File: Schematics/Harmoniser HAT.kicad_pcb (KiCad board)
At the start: 2 copper layers, 98 x 55 mm, 129 parts, among them J1 RPi GPIO, J2 Line In, J3 Inst In, J4 Line Out, J5 Inst Out, J6 I2C Header, J7 PWR, J8 I2S Header, Q1 BC547, Q1 Q_NPN_BEC, Q2 BC547, Q2 Q_NPN_BEC, SW1 RotaryEncoder_Switch, SW2 RotaryEncoder_Switch, SW3 RotaryEncoder_Switch, SW4 RotaryEncoder_Switch, U1 PCM3060, U2 24LC256, U3 Opamp_Dual, U4 Opamp_Dual, U5 PCA9555PW

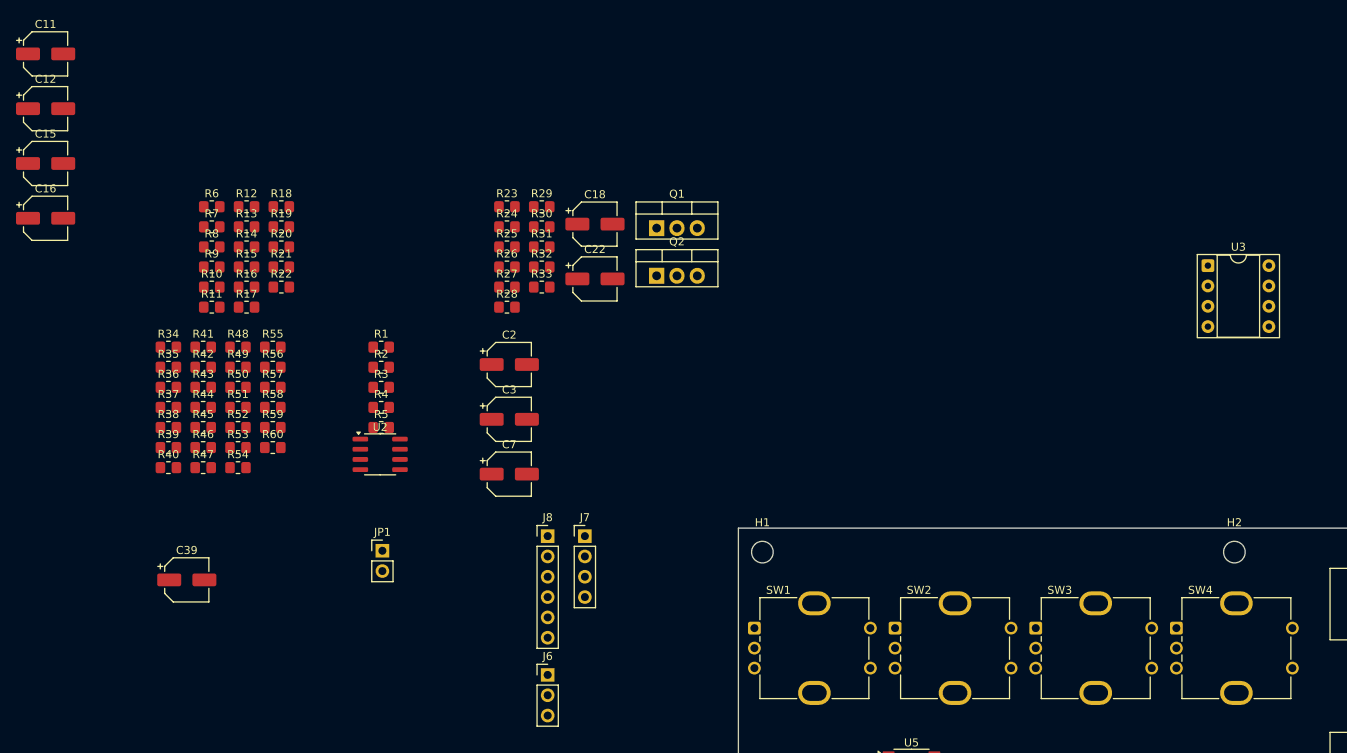
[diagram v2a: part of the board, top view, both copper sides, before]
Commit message: Changed footprints, added 3d model to GPIO
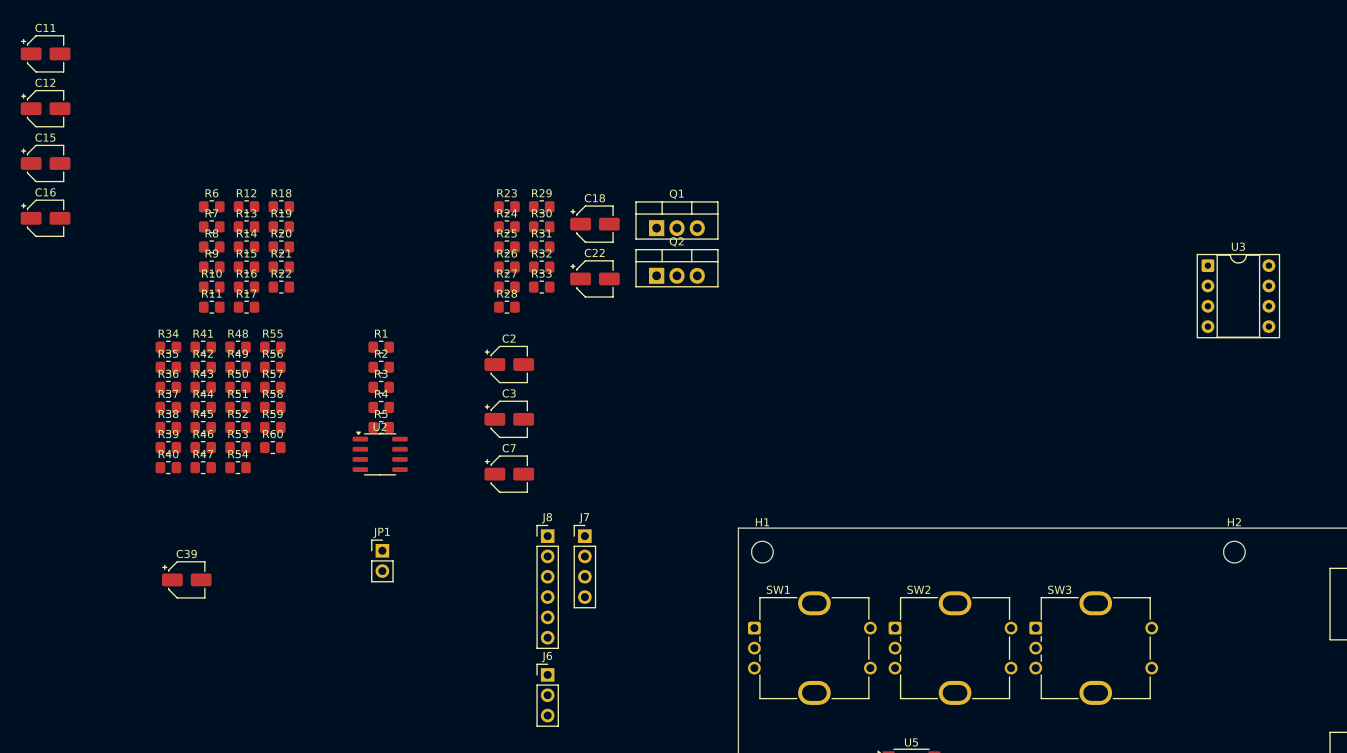
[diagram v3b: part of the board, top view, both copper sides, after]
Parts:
- removed SW4: RotaryEncoder_Switch, Rotary_Encoder:RotaryEncoder_Bourns_Vertical_PEC12R-3x17F-Sxxxx
- C11, C12, C15, C16, C18, C2, C22, C3, C39, C7: footprint Capacitor_SMD:CP_Elec_5x5.4 -> Capacitor_SMD:CP_Elec_4x5.7
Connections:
- U5 pad 18: ENC4_SW -> unconnected-(U5-IO1_5-Pad18)
- U5 pad 19: ENC4_A -> unconnected-(U5-IO1_6-Pad19)
- U5 pad 20: ENC4_B -> unconnected-(U5-IO1_7-Pad20)

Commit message: PCB design start
started on it :)
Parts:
- removed C13, C25, C9: 0.1u, Capacitor_SMD:C_0805_2012Metric_Pad1.18x1.45mm_HandSolder
- removed C26, C27, C28, C29, C30, C31, C32, C33, C34, C35, C36, C37: 0.01u, Capacitor_SMD:C_0805_2012Metric_Pad1.18x1.45mm_HandSolder
- removed the Q1 at (226.2, 27.4)
- removed the Q1 at (96.3, 40.5)
- removed the Q2 at (96.3, 46.5)
- removed the Q2 at (226.2, 33.1)
- removed R40, R41, R42, R43, R44, R45, R49, R50, R51, R52, R53, R54, R55, R56, R57: 10k, Resistor_SMD:R_0805_2012Metric_Pad1.20x1.40mm_HandSolder
- added C40: 0.1u, Capacitor_SMD:C_0805_2012Metric_Pad1.18x1.45mm_HandSolder, F.Cu at (59.3, 130.7)
- added C41: 0.1u, Capacitor_SMD:C_0805_2012Metric_Pad1.18x1.45mm_HandSolder, F.Cu at (164.3, 188.9)
- added C42: 0.1u, Capacitor_SMD:C_0805_2012Metric_Pad1.18x1.45mm_HandSolder, F.Cu at (98.4, 188.9)
- added Q1: BC547, Package_TO_SOT_THT:TO-92_Inline, F.Cu at (110.5, 184.4)
- added Q2: BC547, Package_TO_SOT_THT:TO-92_Inline, F.Cu at (110.5, 190.2)
- moved C5 202.5 mm to (22.2, 122.0)
- moved C6 202.5 mm to (22.2, 127.8)
- moved C1 202.4 mm to (28.5, 120.1)
- moved C4 202.4 mm to (28.5, 123.1)
- moved C8 202.4 mm to (28.5, 126.1)
- moved C11 196.8 mm to (146.3, 169.6)
- moved C12 196.0 mm to (146.3, 175.4)
- moved C15 195.2 mm to (146.3, 181.2)
- moved C16 194.5 mm to (146.3, 187.1)
- moved J6 193.9 mm to (269.2, 149.2)
- moved J8 193.9 mm to (269.2, 131.8)
- moved J7 193.9 mm to (273.9, 131.8)
- moved C17 183.2 mm to (98.4, 170.8)
- moved C19 183.2 mm to (98.4, 173.8)
- moved C21 183.2 mm to (98.4, 179.9)
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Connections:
- SW1 pad A: Net-(R40-Pad2) -> ENC1_A
- SW1 pad B: Net-(R44-Pad2) -> ENC1_B
- SW1 pad S1: Net-(R41-Pad1) -> ENC1_SW
- SW2 pad A: Net-(R42-Pad2) -> ENC2_A
- SW2 pad B: Net-(R45-Pad2) -> ENC2_B
- SW2 pad S1: Net-(R43-Pad1) -> ENC2_SW
- SW3 pad A: Net-(R52-Pad2) -> ENC3_A
- SW3 pad B: Net-(R56-Pad2) -> ENC3_B
- SW3 pad S1: Net-(R53-Pad1) -> ENC3_SW
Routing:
- added copper zone on B.Cu, net GND
- added copper zone on F.Cu, net GND
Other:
- board size 98 x 55 mm -> 1.4 x 13 mm
- board text removed: "OLED DISPLAY"
- board text removed: "Spacings not exact (yet)"

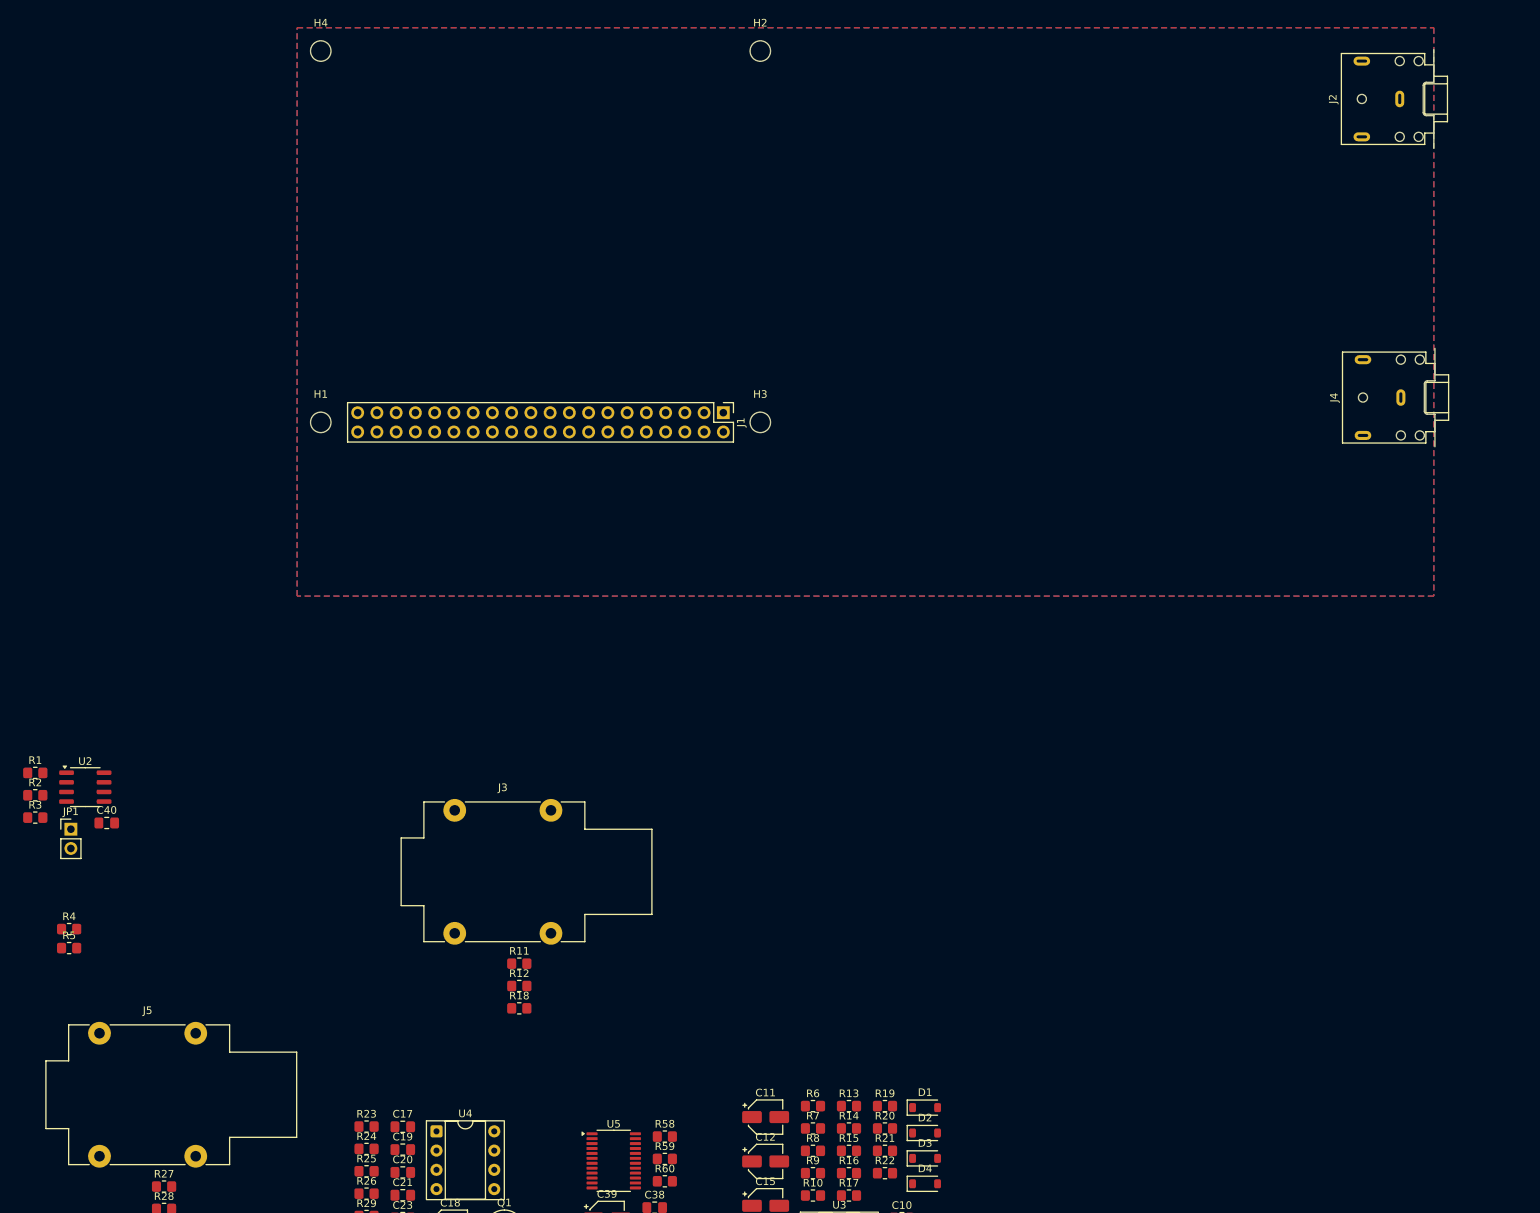
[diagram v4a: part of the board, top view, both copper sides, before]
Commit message: PCB set-up & Jack Sockets
Added 3D file for the Rpi5 and the 1/4" jack sockets. Finalised the dimensions of the PCB with the Pi HAT hole dimensions.
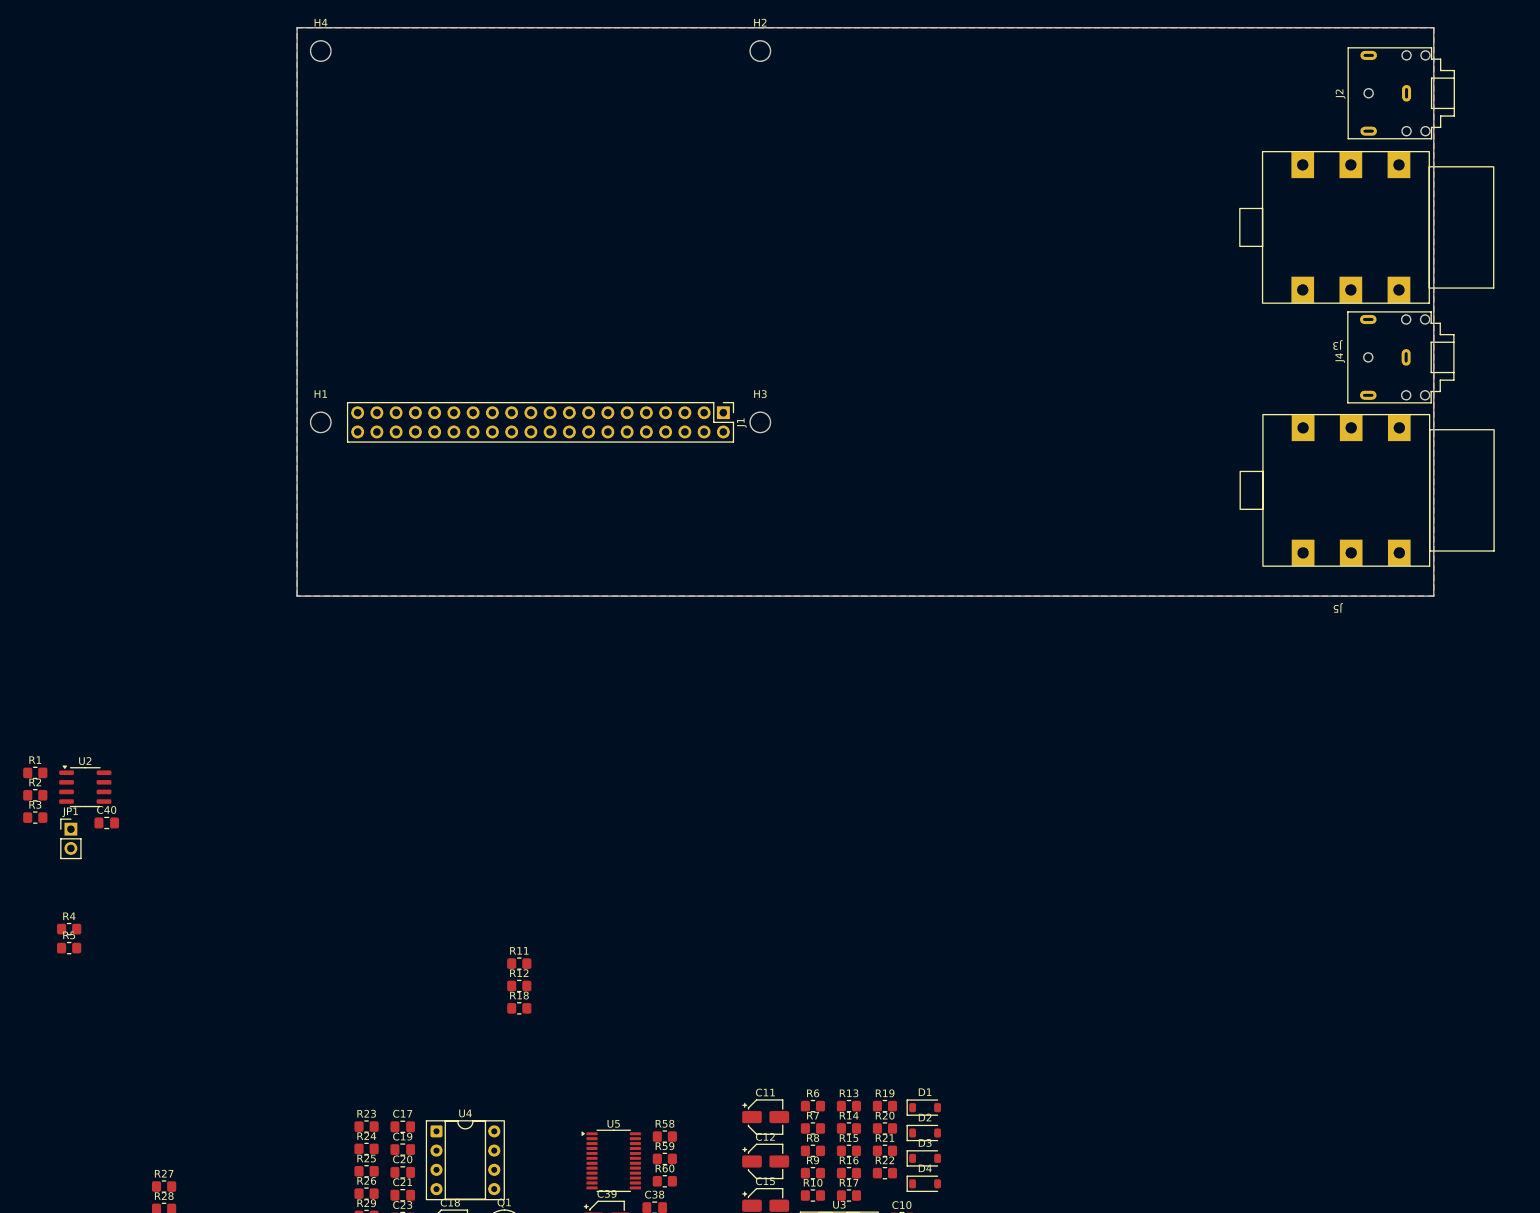
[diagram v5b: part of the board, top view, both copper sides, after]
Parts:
- J3, J5: footprint Connector_Audio:Jack_6.35mm_Neutrik_NMJ4HHD2_Horizontal -> custom:NYS2152G
- moved J5 174.3 mm to (221.4, 96.9), turned to 180 degrees
- moved J3 134.0 mm to (221.3, 62.1), turned to 180 degrees
- moved J4 5.35 mm to (230.8, 69.3)
- moved J2 1.17 mm to (230.8, 34.5)
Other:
- board size 1.4 x 13 mm -> 150 x 75 mm

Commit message: Finished PCB routing
New Layout fits perfectly, now all the parts are through-hole and routed together. 20 Vias is a nightmare but better than what we started with
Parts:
- removed C1, C20, C24, C38, C4, C41, C42, C8: 0.1u, Capacitor_SMD:C_0805_2012Metric_Pad1.18x1.45mm_HandSolder
- removed C10, C14: 330p, Capacitor_SMD:C_0805_2012Metric_Pad1.18x1.45mm_HandSolder
- removed C11, C12, C15, C16, C18, C2, C22, C3, C39, C7: 10u, Capacitor_SMD:CP_Elec_4x5.7
- removed C17, C21: 470p, Capacitor_SMD:C_0805_2012Metric_Pad1.18x1.45mm_HandSolder
- removed C19, C23: 3.3n, Capacitor_SMD:C_0805_2012Metric_Pad1.18x1.45mm_HandSolder
- removed C5, C6: 4.7u, Capacitor_SMD:CP_Elec_4x5.7
- removed D1, D2, D3, D4: 1N4148W, Diode_SMD:D_SOD-123
- removed J2: Line In, Connector_Audio:Jack_3.5mm_CUI_SJ1-3523N_Horizontal
- removed J3: Inst In, custom:NYS2152G
- removed J4: Line Out, Connector_Audio:Jack_3.5mm_CUI_SJ1-3523N_Horizontal
- removed J5: Inst Out, custom:NYS2152G
- removed Q1, Q2: BC547, Package_TO_SOT_THT:TO-92_Inline
- removed R10, R20: 1k, Resistor_SMD:R_0805_2012Metric_Pad1.20x1.40mm_HandSolder
- removed R11, R12, R13, R14, R16, R17, R18, R21, R22, R24, R27, R28, R30, R33, R7, R8: 0, Resistor_SMD:R_0805_2012Metric_Pad1.20x1.40mm_HandSolder
- removed R15: 47k, Resistor_SMD:R_0805_2012Metric_Pad1.20x1.40mm_HandSolder
- removed R19, R25, R31, R5, R58, R59, R60: 10k, Resistor_SMD:R_0805_2012Metric_Pad1.20x1.40mm_HandSolder
- removed R23, R29: 7.5k, Resistor_SMD:R_0805_2012Metric_Pad1.20x1.40mm_HandSolder
- removed R26, R32: 750, Resistor_SMD:R_0805_2012Metric_Pad1.20x1.40mm_HandSolder
- removed R4: 22k, Resistor_SMD:R_0805_2012Metric_Pad1.20x1.40mm_HandSolder
- removed R6, R9: 27k, Resistor_SMD:R_0805_2012Metric_Pad1.20x1.40mm_HandSolder
- removed U1: PCM3060, Package_SO:TSSOP-28_4.4x9.7mm_P0.65mm
- removed U3, U4: Opamp_Dual, Package_DIP:DIP-8_W7.62mm_Socket
- added C13: 100u, Capacitor_THT:CP_Radial_D8.0mm_P5.00mm, F.Cu at (103.5, 52.5)
- added C43: 0.1u, Capacitor_THT:C_Disc_D4.7mm_W2.5mm_P5.00mm, F.Cu at (197.5, 91.0)
- added C9: 100u, Capacitor_THT:CP_Radial_D8.0mm_P5.00mm, F.Cu at (134.4, 52.5)
- added J10: Line In, Connector_Audio:Jack_3.5mm_CUI_SJ1-3523N_Horizontal, F.Cu at (118.5, 47.5)
- added J11: BOB21250-LEFT, Connector_PinSocket_2.54mm:PinSocket_1x16_P2.54mm_Vertical, F.Cu at (149.1, 50.8)
- added J12: BOB21250-RIGHT, Connector_PinSocket_2.54mm:PinSocket_1x16_P2.54mm_Vertical, F.Cu at (172.0, 50.8)
- added J9: Line In, Connector_Audio:Jack_3.5mm_CUI_SJ1-3523N_Horizontal, F.Cu at (91.5, 47.5)
- C40: footprint Capacitor_SMD:C_0805_2012Metric_Pad1.18x1.45mm_HandSolder -> Capacitor_THT:C_Disc_D4.7mm_W2.5mm_P5.00mm
- R1, R2, R3, R34, R35, R36, R37, R38, R39, R46, R47, R48: footprint Resistor_SMD:R_0805_2012Metric_Pad1.20x1.40mm_HandSolder -> Resistor_THT:R_Axial_DIN0207_L6.3mm_D2.5mm_P10.16mm_Horizontal
- U5: value PCA9555PW -> MCP23017_SP; footprint Package_SO:TSSOP-24_4.4x7.8mm_P0.65mm -> Package_DIP:DIP-28_W7.62mm
- moved SW3 212.5 mm to (218.8, 111.0), turned to 180 degrees
- moved R47 204.8 mm to (208.3, 55.5)
- moved R46 201.2 mm to (208.4, 59.5)
- moved R38 196.1 mm to (208.3, 63.5)
- moved R37 192.8 mm to (208.3, 67.5)
- moved R35 188.5 mm to (208.4, 71.5)
- moved R48 186.0 mm to (187.5, 61.5), turned to 180 degrees
- moved R34 185.7 mm to (208.4, 75.5)
- moved SW2 185.2 mm to (195.2, 111.0), turned to 180 degrees
- moved R39 183.4 mm to (187.5, 57.0), turned to 180 degrees
- moved R36 181.0 mm to (187.5, 52.5), turned to 180 degrees
- moved SW1 158.2 mm to (171.8, 111.0), turned to 180 degrees
- moved J8 144.4 mm to (141.5, 64.5), turned to 180 degrees
- moved J7 144.0 mm to (141.5, 75.2)
- moved U5 138.4 mm to (193.7, 54.5)
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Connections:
- J1 pad 11: unconnected-(J1-Pin_11-Pad11) -> INT1
- J1 pad 13: unconnected-(J1-Pin_13-Pad13) -> INT2
- J1 pad 7: MCLK -> unconnected-(J1-Pin_7-Pad7)
- U5 pad 1: INT -> ENC1_SW
- U5 pad 10: unconnected-(U5-IO0_6-Pad10) -> GND
- U5 pad 12: GND -> I2C_SCL
- U5 pad 13: unconnected-(U5-IO1_0-Pad13) -> I2C_SDA
- U5 pad 15: ENC3_SW -> GND
- U5 pad 16: ENC3_A -> GND
- U5 pad 17: ENC3_B -> GND
- U5 pad 18: unconnected-(U5-IO1_5-Pad18) -> +3V3
- U5 pad 19: unconnected-(U5-IO1_6-Pad19) -> INT1
- U5 pad 2: GND -> ENC2_SW
- U5 pad 20: unconnected-(U5-IO1_7-Pad20) -> INT2
- U5 pad 21: GND -> ENC1_A
- U5 pad 22: I2C_SCL -> ENC1_B
- U5 pad 23: I2C_SDA -> ENC2_A
- U5 pad 24: +3V3 -> ENC2_B
- U5 pad 3: GND -> ENC3_SW
- U5 pad 4: ENC1_SW -> unconnected-(U5-GPB3-Pad4)
- U5 pad 5: ENC1_A -> unconnected-(U5-GPB4-Pad5)
- U5 pad 6: ENC1_B -> unconnected-(U5-GPB5-Pad6)
- U5 pad 7: ENC2_SW -> unconnected-(U5-GPB6-Pad7)
- U5 pad 8: ENC2_A -> unconnected-(U5-GPB7-Pad8)
- U5 pad 9: ENC2_B -> +3V3
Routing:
- net +3V3: track 0.00 -> 291.9 mm, vias 0 -> 4
- net INT2: track 0.00 -> 135.3 mm, vias 0 -> 1
- net INT1: track 0.00 -> 128.6 mm, vias 0 -> 1
- net I2C_SCL: track 0.00 -> 118.6 mm, vias 0 -> 1
- net I2S_DOUT: track 0.00 -> 112.7 mm, vias 0 -> 1
- net I2C_SDA: track 0.00 -> 112.3 mm, vias 0 -> 1
- net LIN2: track 0.00 -> 111.4 mm, vias 0 -> 2
- net ENC3_SW: track 0.00 -> 107.7 mm
- net I2S_DIN: track 0.00 -> 102.2 mm, vias 0 -> 1
- net I2S_FS: track 0.00 -> 100.6 mm, vias 0 -> 1
- net OUT_L: track 0.00 -> 95.4 mm
- net RIN2: track 0.00 -> 94.8 mm, vias 0 -> 2
- net ENC2_SW: track 0.00 -> 89.2 mm
- net ENC1_A: track 0.00 -> 88.4 mm
- net I2S_CLK: track 0.00 -> 85.3 mm, vias 0 -> 1
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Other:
- board text added: "ENG5220 - SHRED PEDAL THING"

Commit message: File labelling
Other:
- board text added: "ENG5220 - CHORUS PEDAL"
- board text removed: "ENG5220 - SHRED PEDAL THING"
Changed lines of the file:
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@@
 	)
 	(paper "A4")
+	(title_block
+		(title "Chorsu Pedal PCB")
+		(date "2025-03-12")
+		(rev "v1")
+		(company "DRAWN BY NICOLAS VIALE")
+	)
 	(layers
 		(0 "F.Cu" signal)
@@
 			(fill no)
 			(layer "Cmts.User")
-			(net 6488185)
 		)
 		(fp_circle
@@
 			(fill no)
 			(layer "F.CrtYd")
-			(net 6488185)
 		)
 		(fp_text user "${REFERENCE}"
@@
 			(fill no)
 			(layer "Cmts.User")
-			(net 6488185)
 		)
 		(fp_circle
@@
 			(fill no)
 			(layer "F.CrtYd")
-			(net 6488185)
 		)
 		(fp_text user "${REFERENCE}"
@@
 			(fill no)
 			(layer "Cmts.User")
-			(net 6488185)
 		)
 		(fp_circle
@@
 			(fill no)
 			(layer "F.CrtYd")
-			(net 6488185)
 		)
 		(fp_text user "${REFERENCE}"
@@
 			(fill no)
 			(layer "Cmts.User")
-			(net 6488185)
 		)
 		(fp_circle
@@
 			(fill no)
 			(layer "F.CrtYd")
-			(net 6488185)
 		)
 		(fp_text user "${REFERENCE}"
@@
 		(layer "Edge.Cuts")
 	)
-	(gr_text "ENG5220 - SHRED PEDAL THING"
+	(gr_text "ENG5220 - CHORUS PEDAL"
 		(at 77.5 115 0)
 		(layer "F.Cu")
@@
 		(polygon
 			(pts
-				(xy 77 109.5) (xy 153.5 109.5) (xy 153.5 116) (xy 77 116)
+				(xy 77 109.5) (xy 142 109.5) (xy 142 116) (xy 77 116)
 			)
 		)
